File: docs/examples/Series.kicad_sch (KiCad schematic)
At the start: 2 parts

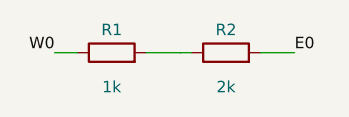
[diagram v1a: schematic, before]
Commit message: ERC-clean KiCad export: project + sym-lib-table, test points on open ports, automatic PWR_FLAGs from geometry nets; ERC (errors+warnings) asserted in tests
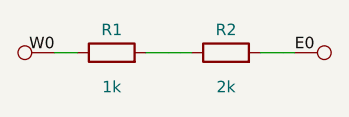
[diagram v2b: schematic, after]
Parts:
- added TP1, TP2: TestPoint, symbol Connector:TestPoint
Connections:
- net E0: now also TP1.1
- net W0: now also TP2.1
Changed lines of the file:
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@@
 		(instances
 			(project "Series"
-				(path "/794dfa40-81ea-46e3-890f-8453cd18027c"
+				(path "/63288836-5431-4726-ace7-3a7b30201adc"
 					(reference "R1")
 					(unit 1)
@@
 		(instances
 			(project "Series"
-				(path "/794dfa40-81ea-46e3-890f-8453cd18027c"
+				(path "/63288836-5431-4726-ace7-3a7b30201adc"
 					(reference "R2")
 					(unit 1)
 				)
+			)
+		)
+	)
+	(symbol
+		(lib_id "Connector:TestPoint")
+		(at 52.07 29.21 270)
+		(unit 1)
+		(exclude_from_sim yes)
+		(in_bom no)
+		(on_board yes)
+		(dnp no)
+		(property "Reference" "TP1"
+			(at 52.07 29.21 90)
+			(effects
+				(font
+					(size 1.27 1.27)
+				)
+				(hide yes)
+			)
+		)
+		(property "Value" "TestPoint"
+			(at 52.07 29.21 90)
+			(effects
+				(font
+					(size 1.27 1.27)
+				)
+				(hide yes)
+			)
+		)
+		(property "Footprint" ""
+			(at 52.07 29.21 90)
+			(effects
+				(font
+					(size 1.27 1.27)
+				)
+				(hide yes)
+			)
+		)
+		(property "Datasheet" ""
+			(at 52.07 29.21 90)
+			(effects
+				(font
+					(size 1.27 1.27)
+				)
+				(hide yes)
+			)
+		)
+		(pin "1"
+		)
+		(instances
+			(project "Series"
+				(path "/63288836-5431-4726-ace7-3a7b30201adc"
+					(reference "TP1")
+					(unit 1)
+				)
+			)
+		)
+	)
+	(symbol
+		(lib_id "Connector:TestPoint")
+		(at 25.4 29.21 90)
+		(unit 1)
+		(exclude_from_sim yes)
+		(in_bom no)
+		(on_board yes)
+		(dnp no)
+		(property "Reference" "TP2"
+			(at 25.4 29.21 90)
+			(effects
+				(font
+					(size 1.27 1.27)
+				)
+				(hide yes)
+			)
+		)
+		(property "Value" "TestPoint"
+			(at 25.4 29.21 90)
+			(effects
+				(font
+					(size 1.27 1.27)
+				)
+				(hide yes)
+			)
+		)
+		(property "Footprint" ""
+			(at 25.4 29.21 90)
+			(effects
+				(font
+					(size 1.27 1.27)
+				)
+				(hide yes)
+			)
+		)
+		(property "Datasheet" ""
+			(at 25.4 29.21 90)
+			(effects
+				(font
+					(size 1.27 1.27)
+				)
+				(hide yes)
+			)
+		)
+		(pin "1"
+		)
+		(instances
+			(project "Series"
+				(path "/63288836-5431-4726-ace7-3a7b30201adc"
+					(reference "TP2")
+					(unit 1)
+				)
